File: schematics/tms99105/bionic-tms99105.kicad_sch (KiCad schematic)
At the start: 6 parts, among them J1 Bionic-P135, J2 Bionic-P245, U1 TMS99105, U2 74HCT126, U3 11AA010-I/TO

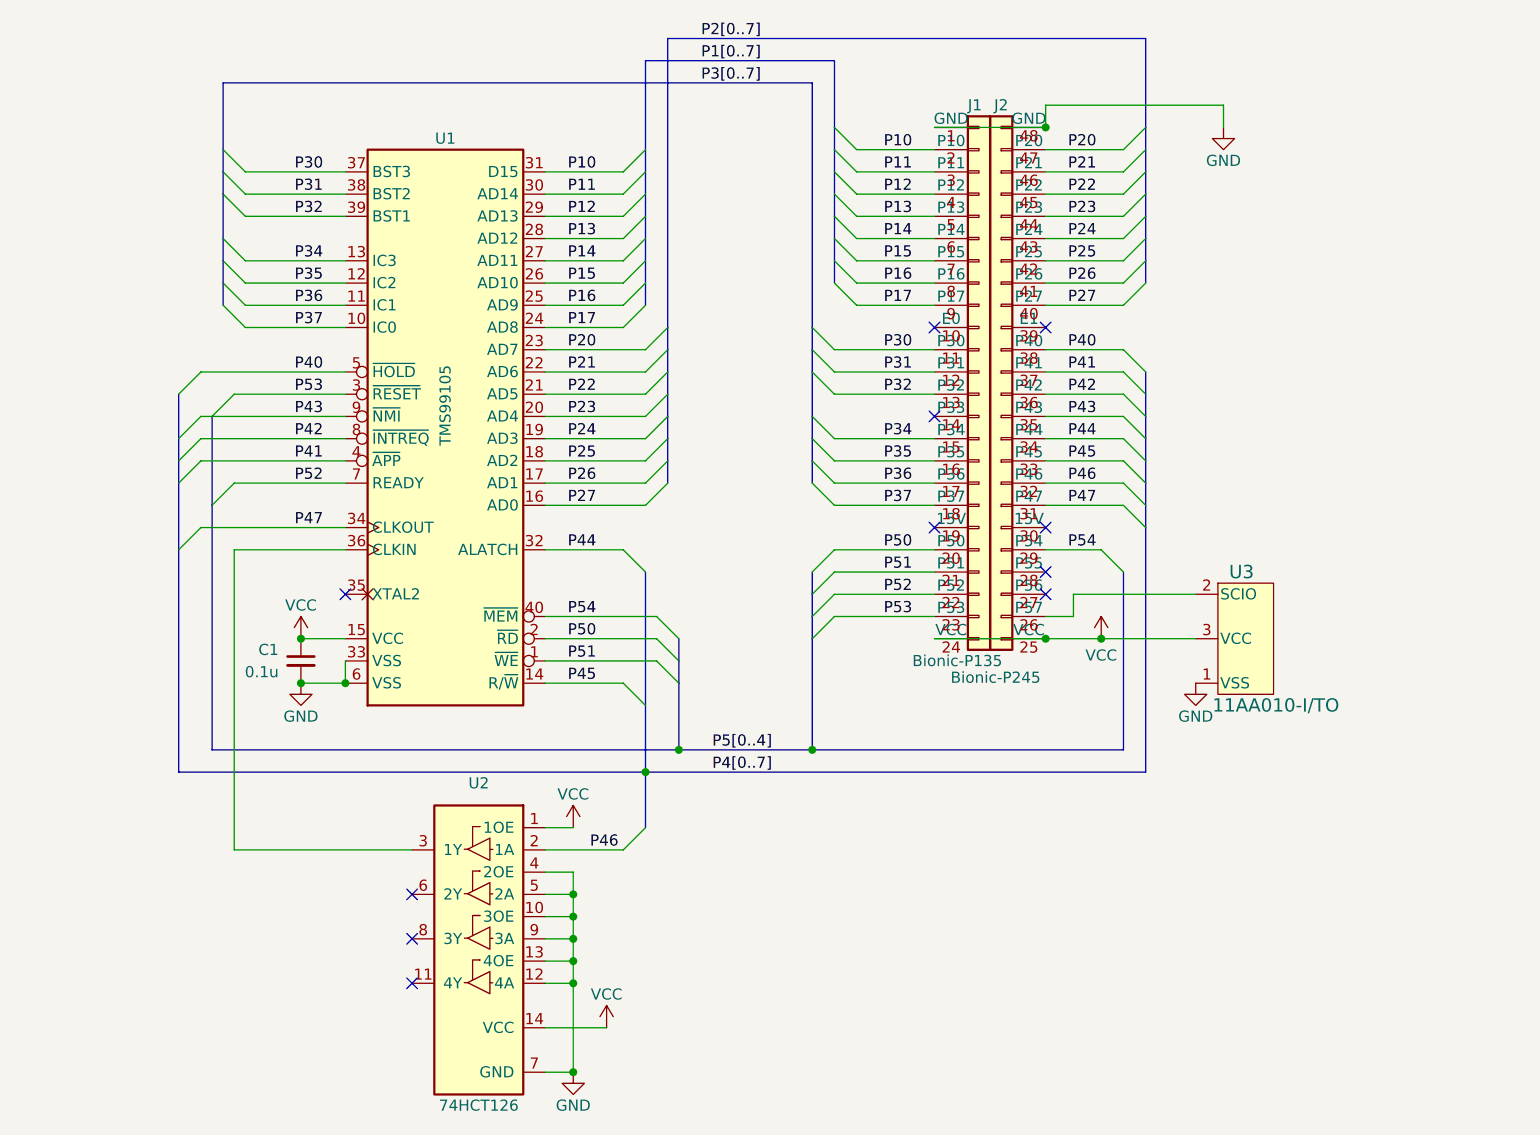
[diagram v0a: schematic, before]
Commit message: [TMS99105] Update schematics
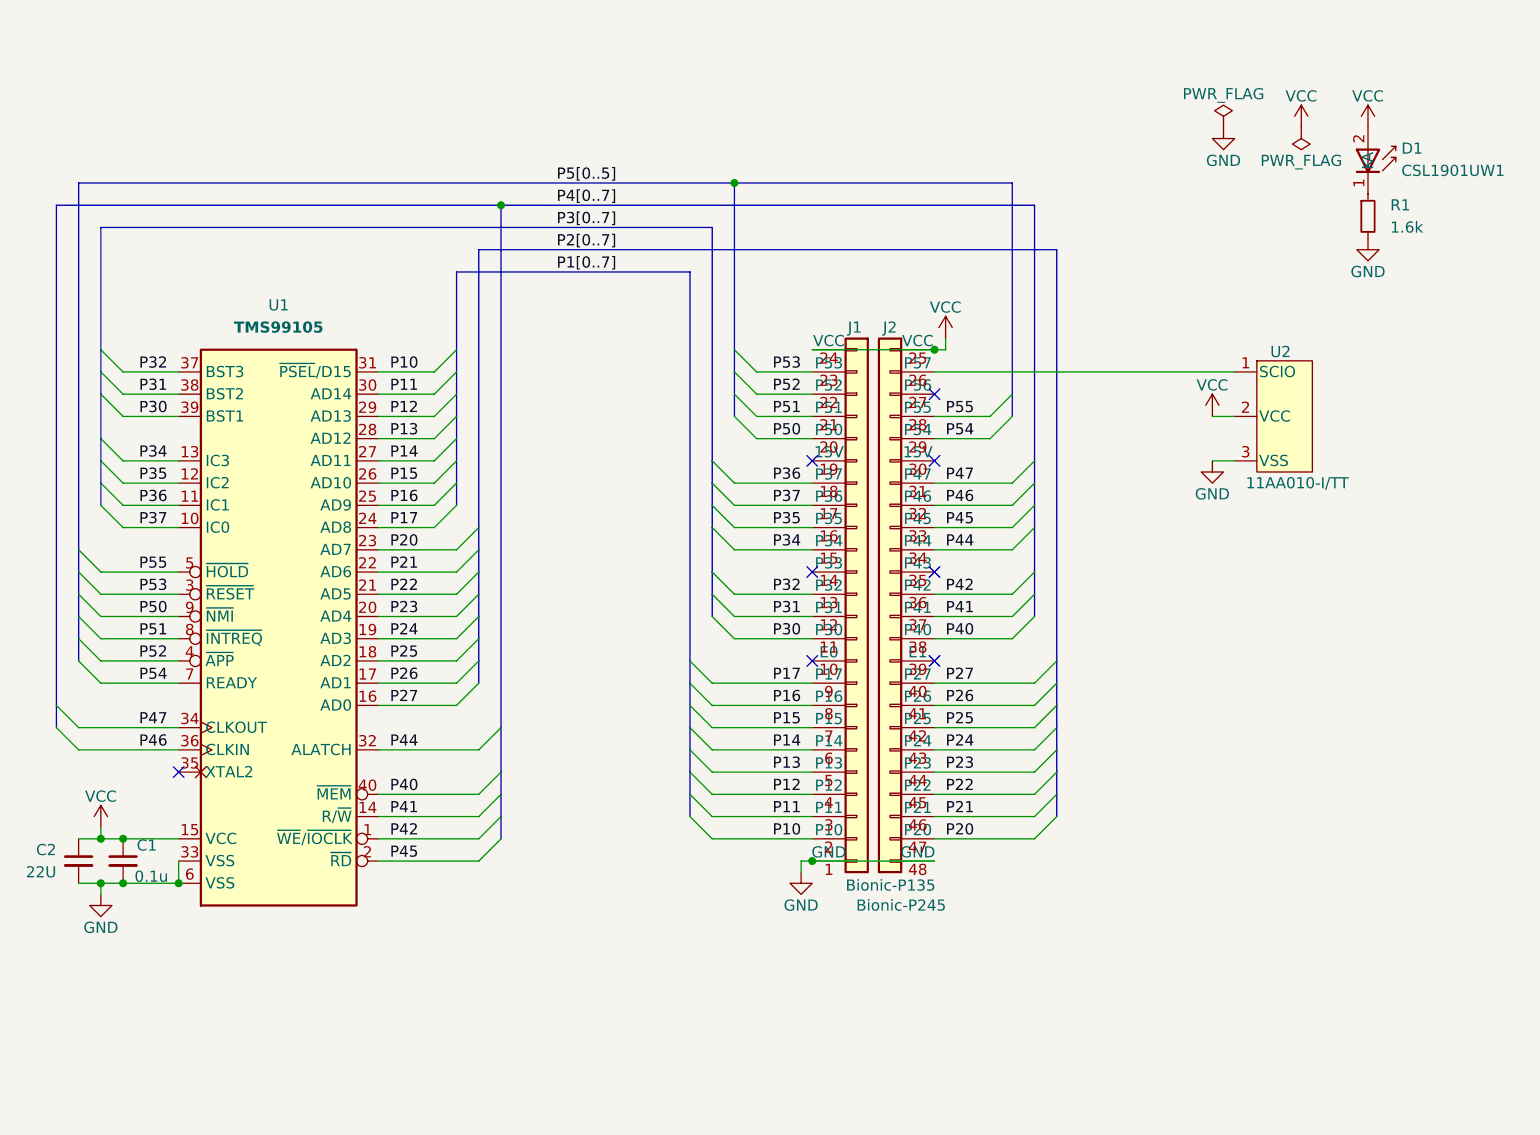
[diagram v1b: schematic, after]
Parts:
- removed U2: 74HCT126, Package_DIP:DIP-14_W7.62mm, symbol 0-LocalLibrary:74HCT126
- removed U3: 11AA010-I/TO, TO-92_MC_MCH, symbol 0-LocalLibrary:11AA010-I_TO
- added C2: 22U, Capacitor_SMD:C_0603_1608Metric_Pad1.08x0.95mm_HandSolder, symbol Device:C_Small
- added D1: CSL1901UW1, 0-LocalLibrary:LED_CSL1901UW1_ROM-M, symbol 0-LocalLibrary:CSL1901UW1
- added R1: 1.6k, Resistor_SMD:R_0603_1608Metric_Pad0.98x0.95mm_HandSolder, symbol Device:R_Small
- added U2: 11AA010-I/TT, 0-LocalLibrary:SOT-23_MC_MCH-M, symbol 0-LocalLibrary:11AA010-I_TT
- C1: footprint Capacitor_THT:C_Disc_D3.4mm_W2.1mm_P2.50mm -> Capacitor_SMD:C_0603_1608Metric_Pad1.08x0.95mm_HandSolder
- J1: footprint connector:Bionic-P135_Vertical -> 0-LocalLibrary:Bionic-P135_Vertical
- J2: footprint connector:Bionic-P245_Vertical -> 0-LocalLibrary:Bionic-P245_Vertical
- U1: footprint Package_DIP:DIP-40_W15.24mm -> 0-LocalLibrary:DIP-40_W15.24mm_Socket
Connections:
- net GND: now also C2.2, R1.2, U2.3 (VSS)
- net P30: now also U1.39 (BST1); no longer U1.37 (BST3)
- net P32: now also U1.37 (BST3); no longer U1.39 (BST1)
- net P36: now also J1.18 (P37); no longer J1.17 (P36)
- net P37: now also J1.17 (P36); no longer J1.18 (P37)
- net P40: now also U1.40 (~{MEM}); no longer U1.5 (~{HOLD})
- net P41: now also U1.14 (R/~{W}); no longer U1.4 (~{APP})
- net P42: now also U1.1 (~{WE}/~{IOCLK}); no longer U1.8 (~{INTREQ})
- net P45: now also U1.2 (~{RD}); no longer U1.14 (R/~{W})
- net P46: now also U1.36 (CLKIN)
- net P50: now also U1.9 (~{NMI}); no longer U1.2 (~{RD})
- net P51: now also U1.8 (~{INTREQ}); no longer U1.1 (~{WE})
- net P52: now also U1.4 (~{APP}); no longer U1.7 (READY)
- net P54: now also U1.7 (READY); no longer U1.40 (~{MEM})
- net VCC: now also C2.1, D1.2 (A), U2.2 (VCC)
- net at J2.26 (P57): now also U2.1 (SCIO)
- net P55: now reaches J2.28 (P55)
- net P55: now also U1.5 (~{HOLD})
- net P43: no longer names the net of J2.35 (P43)
- net P43: no longer U1.9 (~{NMI})
- new net: D1.1 (K), R1.1
- no-connect marks 11 -> 8

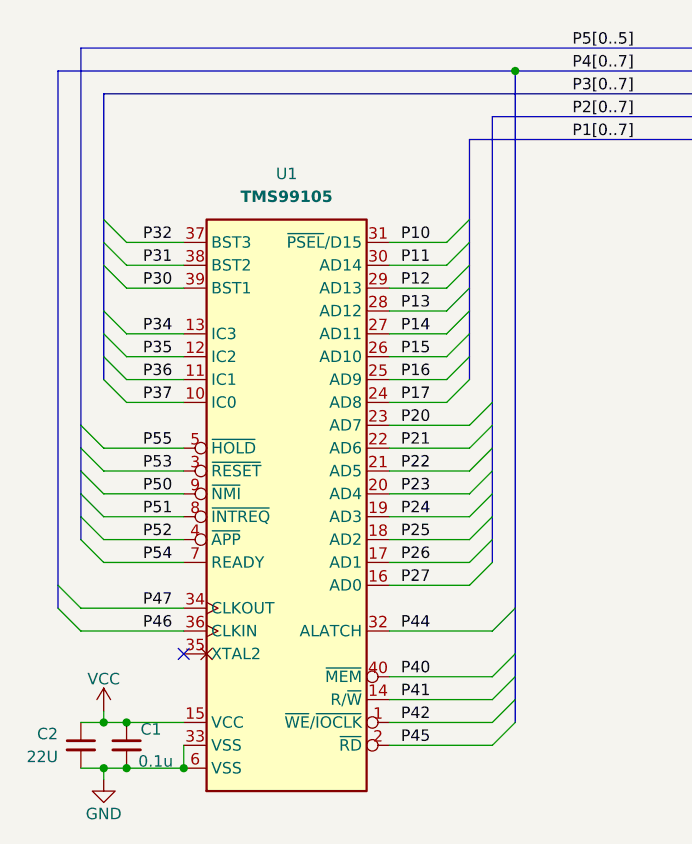
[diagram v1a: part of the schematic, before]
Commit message: [TMS99105] Cleanup schematics
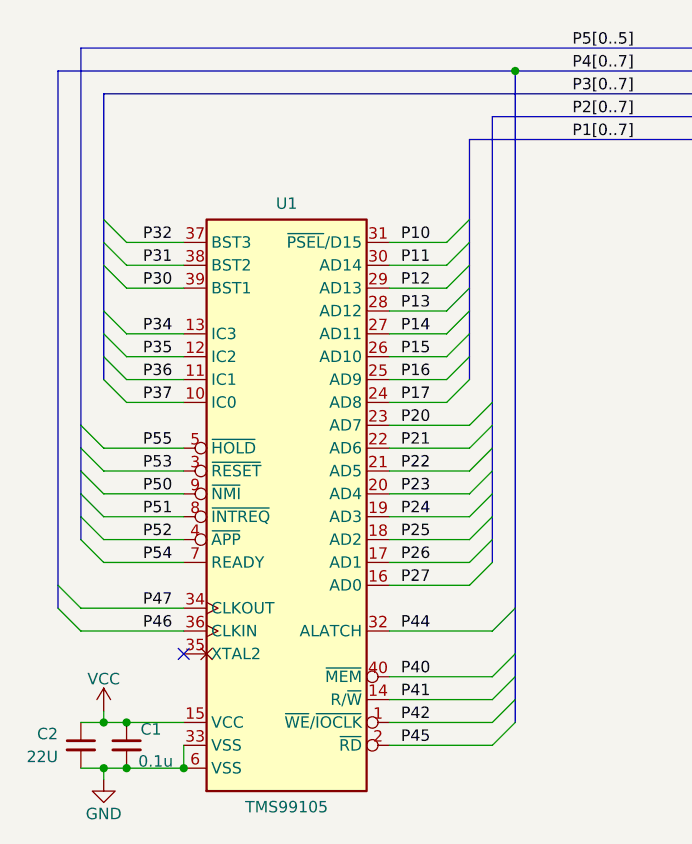
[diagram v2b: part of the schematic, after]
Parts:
- D1: footprint 0-LocalLibrary:LED_CSL1901UW1_ROM-M -> rhom:LED_CSL1901UW1_ROM-M; symbol 0-LocalLibrary:CSL1901UW1 -> rhom:CSL1901UW1
- J1: footprint 0-LocalLibrary:Bionic-P135_Vertical -> bionic:Bionic-P135_Vertical; symbol 0-LocalLibrary:Bionic-P135 -> bionic:Bionic-P135
- J2: footprint 0-LocalLibrary:Bionic-P245_Vertical -> bionic:Bionic-P245_Vertical; symbol 0-LocalLibrary:Bionic-P245 -> bionic:Bionic-P245
- U1: footprint 0-LocalLibrary:DIP-40_W15.24mm_Socket -> bionic:DIP-40_W15.24mm_Socket; symbol 0-LocalLibrary:TMS99105 -> cpu:TMS99105
- U2: footprint 0-LocalLibrary:SOT-23_MC_MCH-M -> microchip:SOT-23_MC_MCH-M; symbol 0-LocalLibrary:11AA010-I_TT -> microchip:11AA010-I_TT
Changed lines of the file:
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@@
 	)
 	(symbol
-		(lib_id "0-LocalLibrary:Bionic-P245")
+		(lib_id "bionic:Bionic-P245")
 		(at 173.99 99.06 0)
 		(unit 1)
@@
 			)
 		)
-		(property "Footprint" "0-LocalLibrary:Bionic-P245_Vertical"
+		(property "Footprint" "bionic:Bionic-P245_Vertical"
 			(at 175.26 134.62 0)
 			(effects
@@
 	)
 	(symbol
-		(lib_id "0-LocalLibrary:11AA010-I_TT")
+		(lib_id "microchip:11AA010-I_TT")
 		(at 212.09 72.39 0)
 		(unit 1)
@@
 			)
 		)
-		(property "Footprint" "0-LocalLibrary:SOT-23_MC_MCH-M"
+		(property "Footprint" "microchip:SOT-23_MC_MCH-M"
 			(at 214.63 90.17 0)
 			(effects
@@
 	)
 	(symbol
-		(lib_id "0-LocalLibrary:Bionic-P135")
+		(lib_id "bionic:Bionic-P135")
 		(at 166.37 99.06 0)
 		(unit 1)
@@
 			)
 		)
-		(property "Footprint" "0-LocalLibrary:Bionic-P135_Vertical"
+		(property "Footprint" "bionic:Bionic-P135_Vertical"
 			(at 167.64 134.62 0)
 			(effects
@@
 	)
 	(symbol
-		(lib_id "0-LocalLibrary:TMS99105")
+		(lib_id "cpu:TMS99105")
 		(at 100.33 101.6 0)
 		(unit 1)
@@
 		(on_board yes)
 		(dnp no)
-		(fields_autoplaced yes)
 		(property "Reference" "U1"
-			(at 100.33 66.04 0)
+			(at 100.33 69.342 0)
 			(effects
 				(font
@@
 		)
 		(property "Value" "TMS99105"
-			(at 100.33 68.58 0)
-			(effects
-				(font
-					(size 1.27 1.27)
-					(bold yes)
-				)
-			)
-		)
-		(property "Footprint" "0-LocalLibrary:DIP-40_W15.24mm_Socket"
-			(at 101.6 135.89 0)
+			(at 100.33 136.398 0)
+			(effects
+				(font
+					(size 1.27 1.27)
+				)
+			)
+		)
+		(property "Footprint" "bionic:DIP-40_W15.24mm_Socket"
+			(at 100.33 144.526 0)
 			(effects
 				(font
@@
 	)
 	(symbol
-		(lib_id "0-LocalLibrary:CSL1901UW1")
+		(lib_id "rhom:CSL1901UW1")
 		(at 224.79 45.72 270)
 		(unit 1)
@@
 			)
 		)
-		(property "Footprint" "0-LocalLibrary:LED_CSL1901UW1_ROM-M"
+		(property "Footprint" "rhom:LED_CSL1901UW1_ROM-M"
 			(at 215.9 49.53 0)
 			(effects

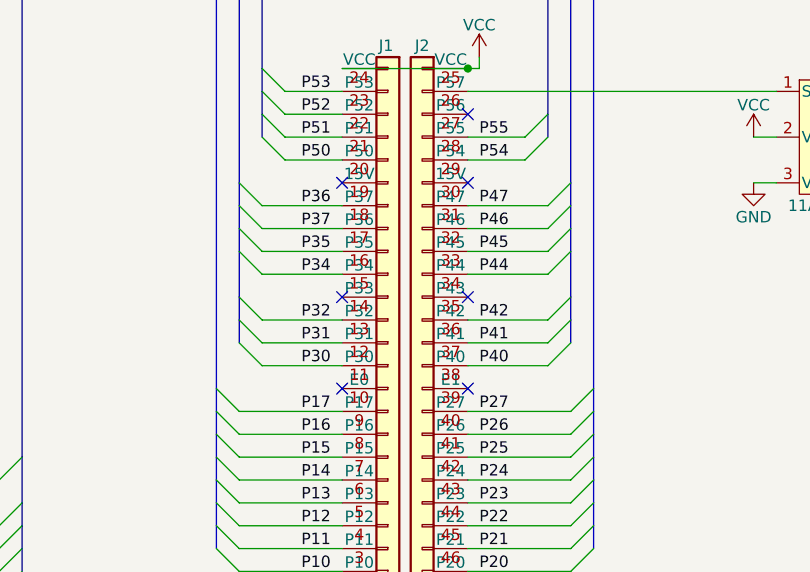
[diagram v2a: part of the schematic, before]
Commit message: [TMS99105] Update schematics
Remove unused pins from bionic connector
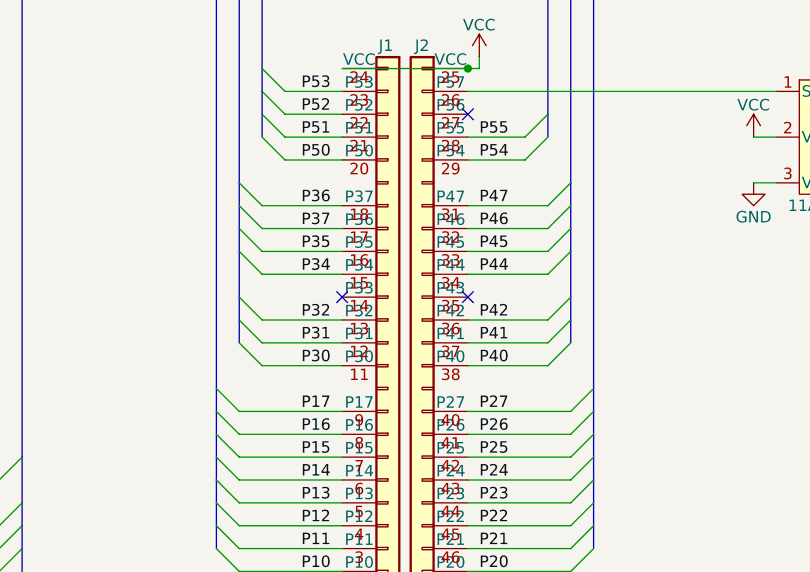
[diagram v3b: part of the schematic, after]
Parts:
- J1: footprint bionic:Bionic-P135_Vertical -> bionic:Bionic-P135_THT
- J2: footprint bionic:Bionic-P245_Vertical -> bionic:Bionic-P245_THT
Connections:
- no-connect marks 8 -> 4
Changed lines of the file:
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@@
 	(title_block
 		(title "BionicTMS99105")
-		(date "2024-12-28")
-		(rev "2")
+		(date "2025-03-02")
+		(rev "3")
 		(company "Tadashi G. Takaoka")
 	)
@@
 	)
 	(no_connect
-		(at 161.29 106.68)
-	)
-	(no_connect
 		(at 175.26 96.52)
 	)
@@
 	)
 	(no_connect
-		(at 161.29 83.82)
-	)
-	(no_connect
 		(at 88.9 119.38)
 	)
 	(no_connect
-		(at 175.26 83.82)
-	)
-	(no_connect
 		(at 161.29 96.52)
 	)
-	(no_connect
-		(at 175.26 106.68)
-	)
 	(bus_entry
 		(at 147.32 119.38)
@@
 			)
 		)
-		(property "Footprint" "bionic:Bionic-P245_Vertical"
+		(property "Footprint" "bionic:Bionic-P245_THT"
 			(at 175.26 134.62 0)
 			(effects
@@
 		(pin "31"
 		)
-		(pin "30"
-		)
-		(pin "39"
-		)
 		(pin "37"
 		)
@@
 			)
 		)
-		(property "Footprint" "bionic:Bionic-P135_Vertical"
+		(property "Footprint" "bionic:Bionic-P135_THT"
 			(at 167.64 134.62 0)
 			(effects
@@
 		(pin "13"
 		)
-		(pin "19"
-		)
 		(pin "15"
 		)
-		(pin "10"
-		)
 		(pin "1"
